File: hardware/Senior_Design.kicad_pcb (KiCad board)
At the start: 4 copper layers, 144 x 146 mm, 154 parts, among them IC301 TLV61220DBVT, J201 Conn_ARM_JTAG_SWD_10, J301 54-00125, J302 Conn_01x03, J401 Conn_ARM_JTAG_SWD_10, J601 2305018-2, J701 J0011D21BNL, Q301 CSD87503Q3E, Q302 Q_NMOS, Q303 CSD87503Q3E, SW201 SW_Push, SW401 SW_Push, U201 EFR32FG28A122F1024GM48-A, U202 USBLC6-2P6, U203 USBLC6-2P6, U301 BQ25798RQMR, U302 TPS63020DSJR, U401 BDE-MB1352P71UA32, U402 USBLC6-2P6, U403 USBLC6-2P6, U501 BME688, U502 USBLC6-2P6, U601 CP2102N-A02-GQFN20, U602 CDSOT236-0504C, U701 W5500, Y201 LF_Crystal, Y202 ECS-390-CDX-1932, Y701 ECS-250-18-5PX-F-TR

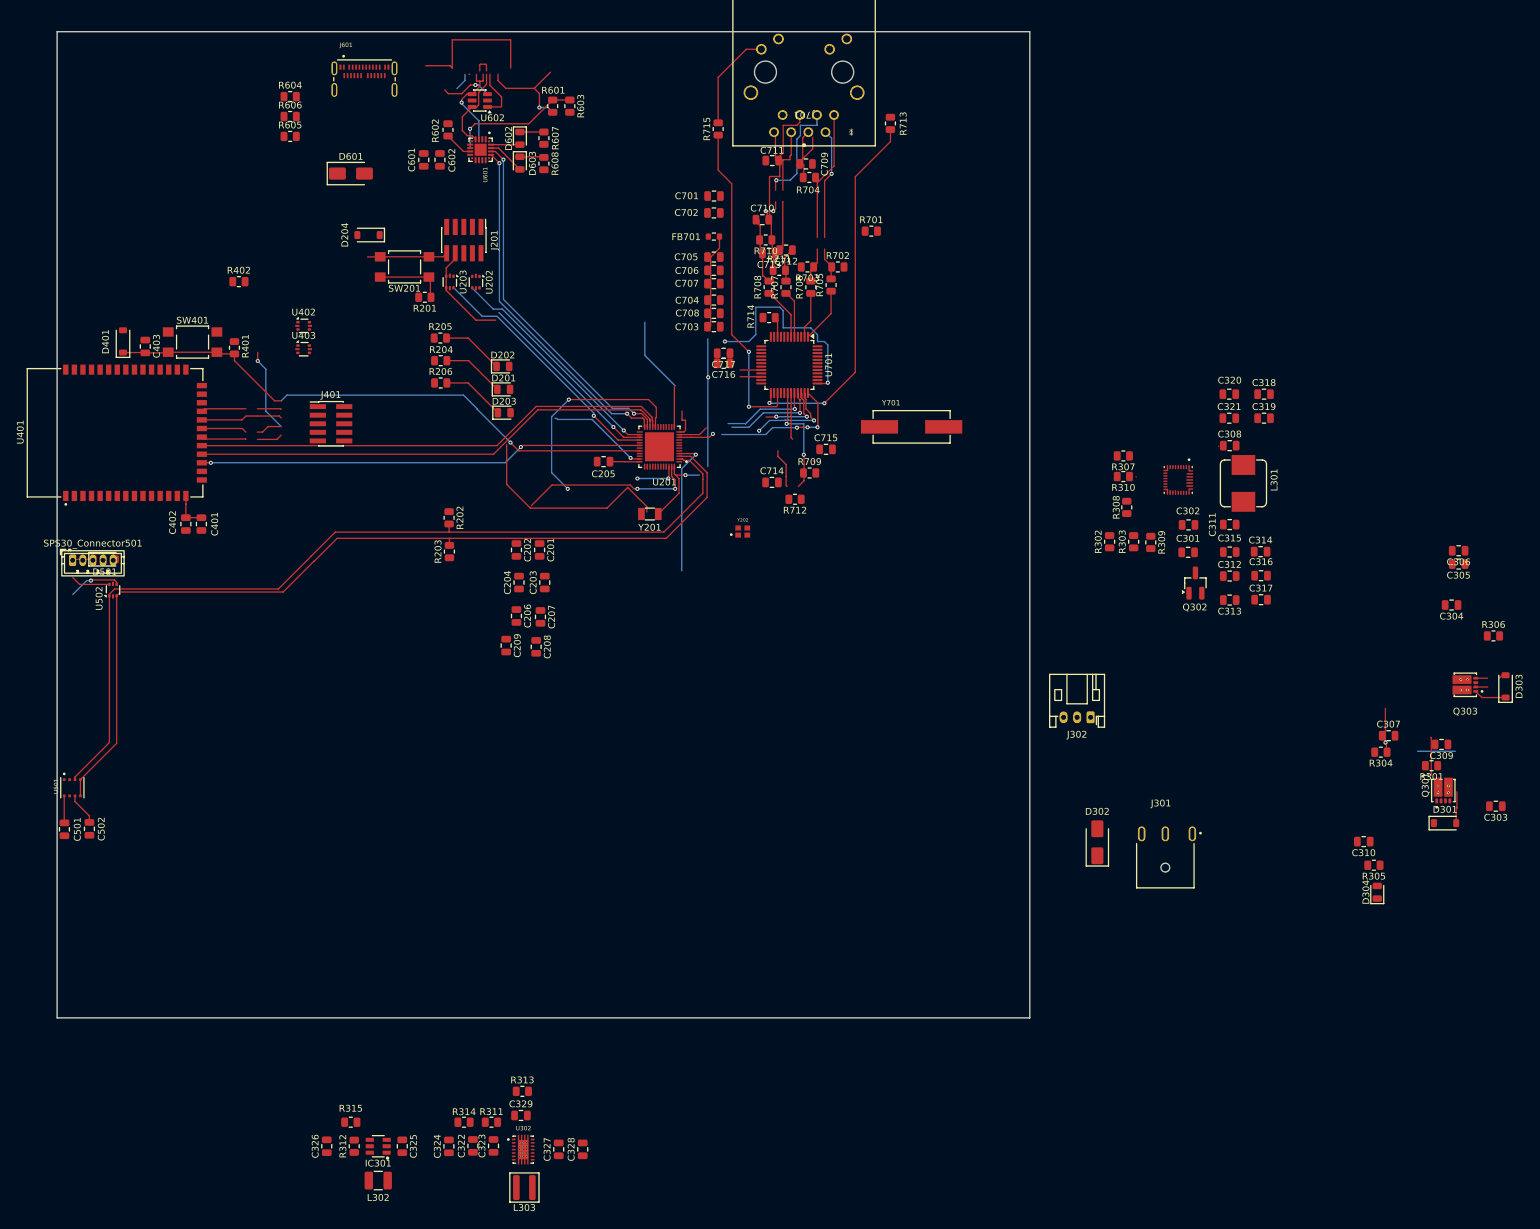
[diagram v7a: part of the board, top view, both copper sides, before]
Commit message: added QON pushbutton
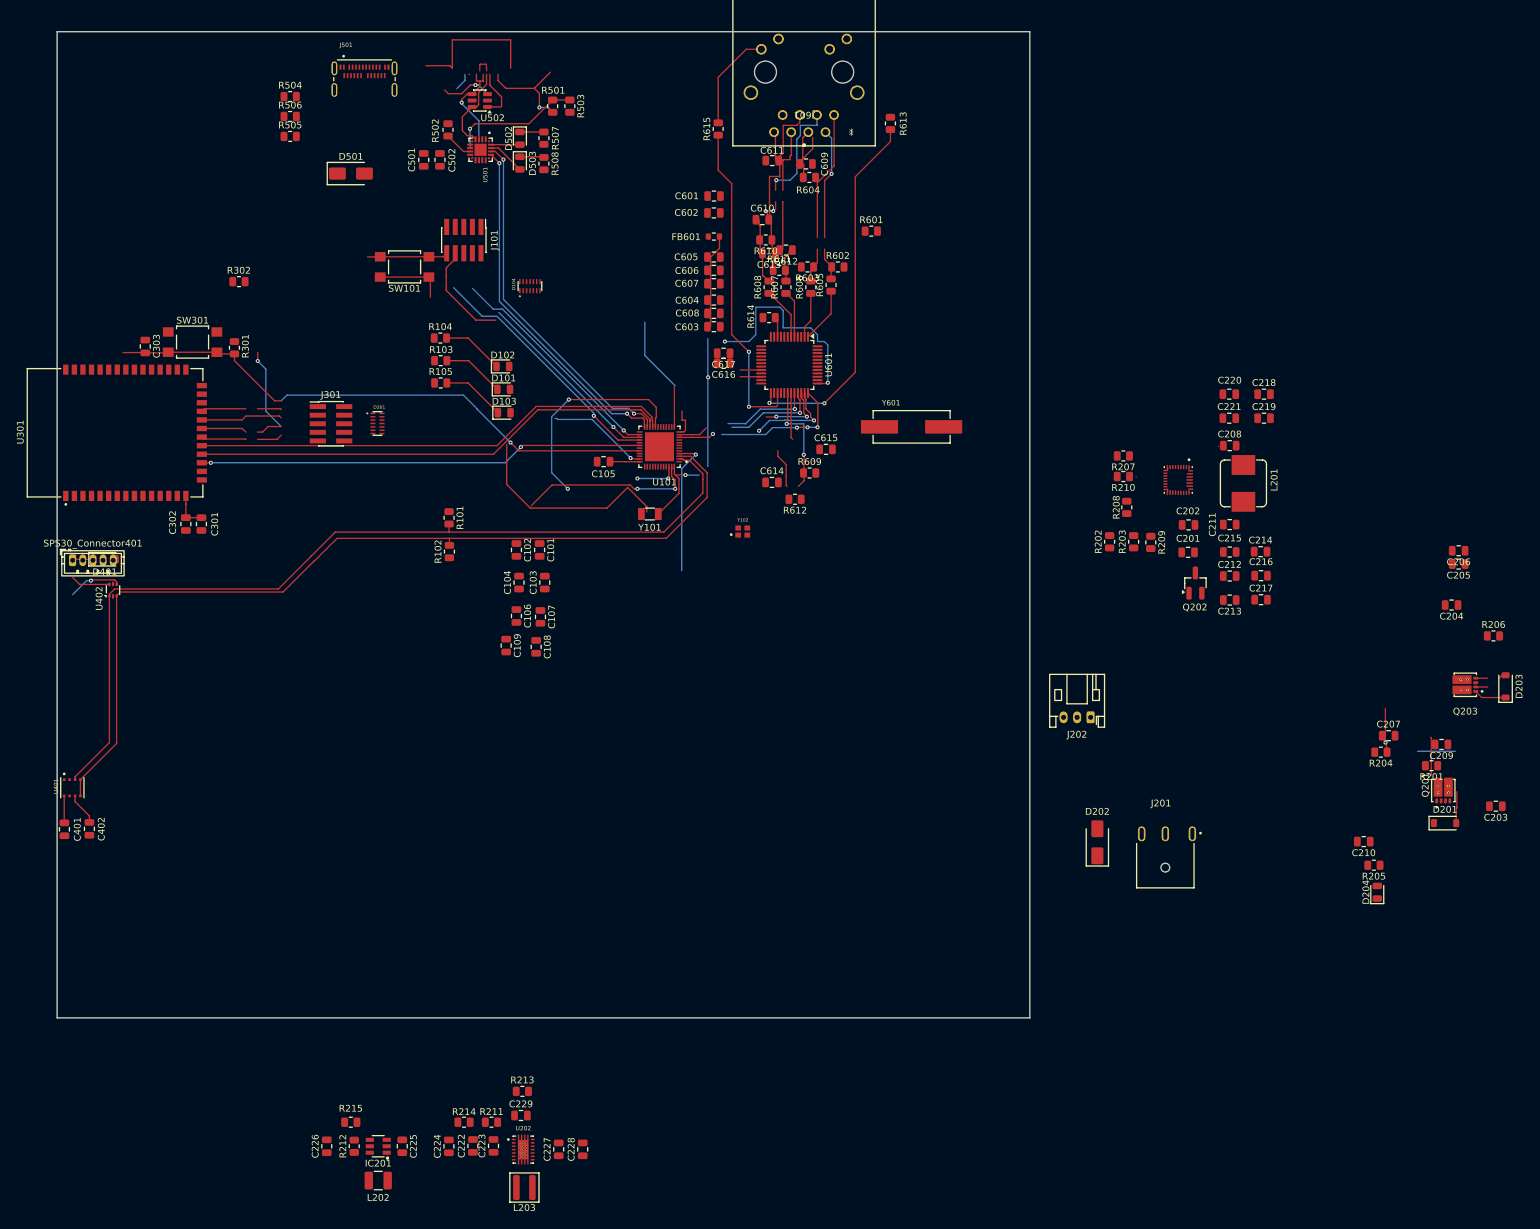
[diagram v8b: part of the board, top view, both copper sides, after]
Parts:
- removed the D204 at (69.1, 50.1)
- removed the D401 at (32.8, 65.8)
- removed the R201 at (77.4, 59.3)
- removed the U202 at (85.0, 57.1)
- removed U203, U403: USBLC6-2P6, Package_TO_SOT_SMD:SOT-666
- removed the U402 at (59.5, 63.5)
- added D104: TPD6E05U06RVZR, pyronet_footprints:SON50P135X350X55-14N, F.Cu at (93.0, 57.7)
- added D301: TPD6E05U06RVZR, pyronet_footprints:SON50P135X350X55-14N, F.Cu at (70.4, 78.0)
- renumbered C201 to C101, C202 to C102, C203 to C103, C204 to C104, C205 to C105, C206 to C106, C207 to C107, C208 to C108, C209 to C109, C301 to C201, C302 to C202, C303 to C203, C304 to C204, C305 to C205, C306 to C206, C307 to C207, C308 to C208, C309 to C209, C310 to C210, C311 to C211, C312 to C212, C313 to C213, C314 to C214, C315 to C215, C316 to C216, C317 to C217, C318 to C218, C319 to C219, C320 to C220, C321 to C221, C322 to C222, C323 to C223, C324 to C224, C325 to C225, C326 to C226, C327 to C227, C328 to C228, C329 to C229, C401 to C301, C402 to C302, C403 to C303, C501 to C401, C502 to C402, C601 to C501, C602 to C502, C701 to C601, C702 to C602, C703 to C603, C704 to C604, C705 to C605, C706 to C606, C707 to C607, C708 to C608, C709 to C609, C710 to C610, C711 to C611, C712 to C612, C713 to C613, C714 to C614, C715 to C615, C716 to C616, C717 to C617, D201 to D101, D202 to D102, D203 to D103, D301 to D201, D302 to D202, D303 to D203, D304 to D204, D501 to D401, D601 to D501, D602 to D502, D603 to D503, FB701 to FB601, IC301 to IC201, J201 to J101, J301 to J201, J302 to J202, J401 to J301, J601 to J501, J701 to J601, L301 to L201, L302 to L202, L303 to L203, Q301 to Q201, Q302 to Q202, Q303 to Q203, R202 to R101, R203 to R102, R204 to R103, R205 to R104, R206 to R105, R301 to R201, R302 to R202, R303 to R203, R304 to R204, R305 to R205, R306 to R206, R307 to R207, R308 to R208, R309 to R209, R310 to R210, R311 to R211, R312 to R212, R313 to R213, R314 to R214, R315 to R215, R401 to R301, R402 to R302, R601 to R501, R602 to R502, R603 to R503, R604 to R504, R605 to R505, R606 to R506, R607 to R507, R608 to R508, R701 to R601, R702 to R602, R703 to R603, R704 to R604, R705 to R605, R706 to R606, R707 to R607, R708 to R608, R709 to R609, R710 to R610, R711 to R611, R712 to R612, R713 to R613, R714 to R614, R715 to R615, SPS30_Connector501 to SPS30_Connector401, SW201 to SW101, SW401 to SW301, U201 to U101, U301 to U201, U302 to U202, U401 to U301, U501 to U401, U502 to U402, U601 to U501, U602 to U502, U701 to U601, Y201 to Y101, Y202 to Y102, Y701 to Y601
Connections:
- net /Ethernet/CS renamed /Ethernet/SPI_CS
- C303 pad 1: /Wi-SUN Module/BDE_RST -> /MCU/BDE_RST
- J301 pad 10: /Wi-SUN Module/BDE_RST -> /MCU/BDE_RST
- R301 pad 2: /Wi-SUN Module/BDE_RST -> /MCU/BDE_RST
- SW101 pad 1: Net-(R201-Pad1) -> GND
- SW301 pad 2: /Wi-SUN Module/BDE_RST -> /MCU/BDE_RST
- U101 pad 10: /MCU/W5500_INT -> /Ethernet/W5500_INT
- U101 pad 32: /MCU/BDE_RESET -> /MCU/BDE_RST
- U101 pad 9: /MCU/W5500_RST -> /Ethernet/W5500_RST
- U301 pad 30: /Wi-SUN Module/BDE_RST -> /MCU/BDE_RST
- U601 pad 36: /Ethernet/INT1 -> /Ethernet/W5500_INT
- U601 pad 37: /Ethernet/W550_RST -> /Ethernet/W5500_RST
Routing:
- net /MCU/BDE_RST: track 0.00 -> 83.9 mm, vias 0 -> 1
- net /MCU/BDE_RESET: track 56.9 -> 0.00 mm, vias 1 -> 0
- net /Ethernet/W550_RST: track 31.3 -> 0.00 mm, vias 2 -> 0
- net /Ethernet/W5500_RST: track 0.00 -> 31.3 mm, vias 0 -> 2
- net /Wi-SUN Module/BDE_RST: track 27.1 -> 0.00 mm
- net /Ethernet/W5500_INT: track 0.00 -> 25.5 mm, vias 0 -> 4
- net /Ethernet/INT1: track 20.3 -> 0.00 mm, vias 3 -> 0
- net GND: track 9.89 -> 20.2 mm
- net Net-(R201-Pad1): track 10.3 -> 0.00 mm
- net /MCU/W5500_INT: track 5.19 -> 0.00 mm, vias 1 -> 0
